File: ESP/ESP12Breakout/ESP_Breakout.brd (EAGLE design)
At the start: 33 x 52.1 mm, 15 parts, among them U1 AMS1117-3.3, X2 ESP-12

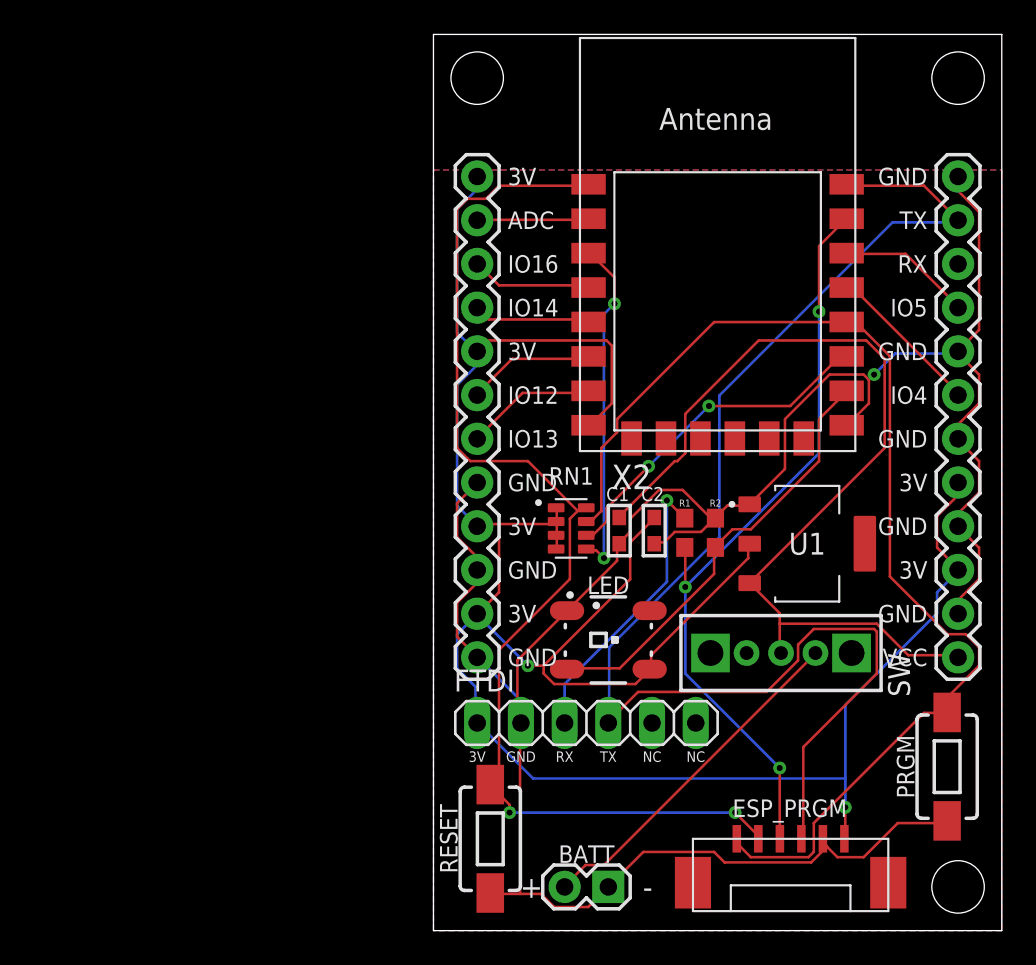
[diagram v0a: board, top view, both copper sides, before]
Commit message: update usb & Arduino pro mini
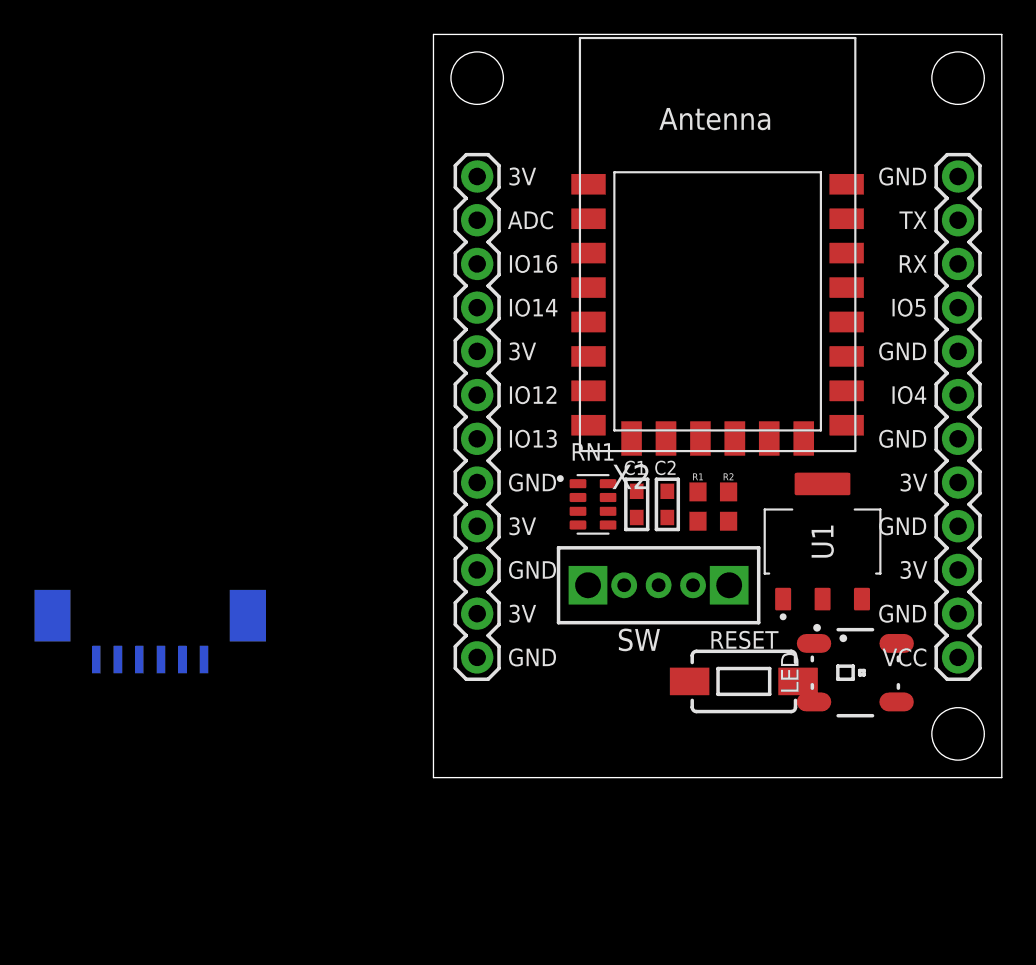
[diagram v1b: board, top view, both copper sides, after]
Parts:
- removed BATT: BATTERY_THD_+-, AutoPark:1X02_PLUS_MINUS
- removed ESP_PRGM: JST_1.25_6P, Scott-Connectors:JST1.25_6P
- removed FTDI: (no value), pinhead:1X06
- removed PRGM: PUSHBUTTON, AutoPark:TACTILE_SWITCH_SMD_6.0X3.5MM
- added PROGRAMMER: JST_1.25_6P, Scott-Connectors:JST1.25_6P
- R2: value 4.7K -> 330
- moved RESET 17.3 mm to (18.0, 14.5), turned to 0 degrees
- moved LED 14.5 mm to (24.5, 15.0)
- moved SW 8.13 mm to (13.1, 20.1)
- moved RN1 1.89 mm to (9.27, 24.8)
- moved C1 1.83 mm to (11.8, 24.8)
- moved C2 1.70 mm to (13.6, 24.8)
- moved R1 1.70 mm to (15.4, 24.6)
- moved R2 1.70 mm to (17.1, 24.6)
- moved U1 0.90 mm to (22.6, 22.6), turned to 0 degrees
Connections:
- new net N$2: LED.DIN, R2.2
- net 3.3V: now also PROGRAMMER.6; no longer ESP_PRGM.1, FTDI.1, RN1.1
- net GND: now also PROGRAMMER.5, RN1.1; no longer BATT.-, ESP_PRGM.2, FTDI.2, PRGM.1, R2.1
- net GPIO0: now also PROGRAMMER.1; no longer ESP_PRGM.6, PRGM.2, RN1.7
- net GPIO15: now also R2.1, RN1.8; no longer LED.DIN, R2.2
- net N$1: no longer BATT.+
- net RESET: now also PROGRAMMER.2, RN1.7; no longer ESP_PRGM.5, RN1.8
- net RXD: now also PROGRAMMER.4; no longer ESP_PRGM.4
- net TXD: now also PROGRAMMER.3; no longer ESP_PRGM.3, FTDI.4
- net USB_RX: no longer FTDI.3
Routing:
- net 3.3V: track 136.6 -> 0.00 mm, vias 2 -> 0
- net GND: track 135.9 -> 0.00 mm, vias 1 -> 0
- net TXD: track 79.6 -> 0.00 mm
- net GPIO0: track 67.4 -> 0.00 mm
- net RESET: track 66.6 -> 0.00 mm, vias 2 -> 0
- net VBAT: track 53.8 -> 0.00 mm
- net RXD: track 44.5 -> 0.00 mm, vias 3 -> 0
- net GPIO15: track 25.3 -> 0.00 mm
- net N$1: track 20.2 -> 0.00 mm
- net GPIO2: track 19.9 -> 0.00 mm, vias 2 -> 0
- net CH_PD: track 19.9 -> 0.00 mm, vias 2 -> 0
- net USB_RX: track 16.9 -> 0.00 mm, vias 1 -> 0
- net GPIO4/SDA: track 9.13 -> 0.00 mm
- net GPIO5/SCL: track 7.82 -> 0.00 mm
- net GPIO13/MOSI: track 7.69 -> 0.00 mm
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- removed copper zone on layer 1, net GND
- removed copper zone on layer 16, net GND
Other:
- board size 33 x 52.1 mm -> 33 x 43.2 mm
- board text added: "ESP12 Breakout V3 Apr 8, 2019"
- board text removed: "3V"
- board text removed: "ESP12 Breakout V2 Mar 25, 2019"
- board text removed: "GND"
- board text removed: "NC"
- board text removed: "RX"
- board text removed: "TX"
